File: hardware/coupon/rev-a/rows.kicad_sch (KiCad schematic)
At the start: 71 parts, among them Q1 DMP2066LSN-7, Q10 DMP2066LSN-7, Q11 DMP2066LSN-7, Q12 DMP2066LSN-7, Q13 DMP2066LSN-7, Q14 DMP2066LSN-7, Q15 DMP2066LSN-7, Q16 DMP2066LSN-7, Q17 2N7002K-7, Q18 2N7002K-7, Q19 2N7002K-7, Q2 DMP2066LSN-7, Q20 2N7002K-7, Q21 2N7002K-7, Q22 2N7002K-7, Q23 2N7002K-7, Q24 2N7002K-7, Q25 2N7002K-7, Q26 2N7002K-7, Q27 2N7002K-7, Q28 2N7002K-7, Q29 2N7002K-7, Q3 DMP2066LSN-7, Q30 2N7002K-7, Q31 2N7002K-7, Q32 2N7002K-7, Q4 DMP2066LSN-7, Q5 DMP2066LSN-7, Q6 DMP2066LSN-7, Q7 DMP2066LSN-7, Q8 DMP2066LSN-7, Q9 DMP2066LSN-7, U2 74HC4514PW,118

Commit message: Accept corrected power-library review and clear row schematic title block
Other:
- note added: "Never fabricate from this sheet alone. Real rails, VLED interlock, DRC/DFM, Gate A and timing/ghosting tests remain."
- note removed: "Never fabricate from this sheet alone. Controller, real rails, DRC/DFM, Gate A and coupon timing/ghosting tests remain."
- moved on the sheet: Q10, Q11, Q12, Q13, Q14, Q15, Q16, Q21, Q22, Q23, Q24, Q25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

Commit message: Normalize Panasonic ERJ order codes across coupon
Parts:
- R10, R11, R12, R13, R14, R15, R16, R17, R18, R19, R20, R21, R6, R7, R8, R9: symbol rgb-badge-coupon:ERJ-2RKF1001X -> rgb-badge-coupon:ERJ2RKF1001X; MPN ERJ-2RKF1001X -> ERJ2RKF1001X
- R22, R23, R24, R25, R26, R27, R28, R29, R30, R31, R32, R33, R34, R35, R36, R37, R38, R39, R40, R41, R42: symbol rgb-badge-coupon:ERJ-2RKF1003X -> rgb-badge-coupon:ERJ2RKF1003X; MPN ERJ-2RKF1003X -> ERJ2RKF1003X

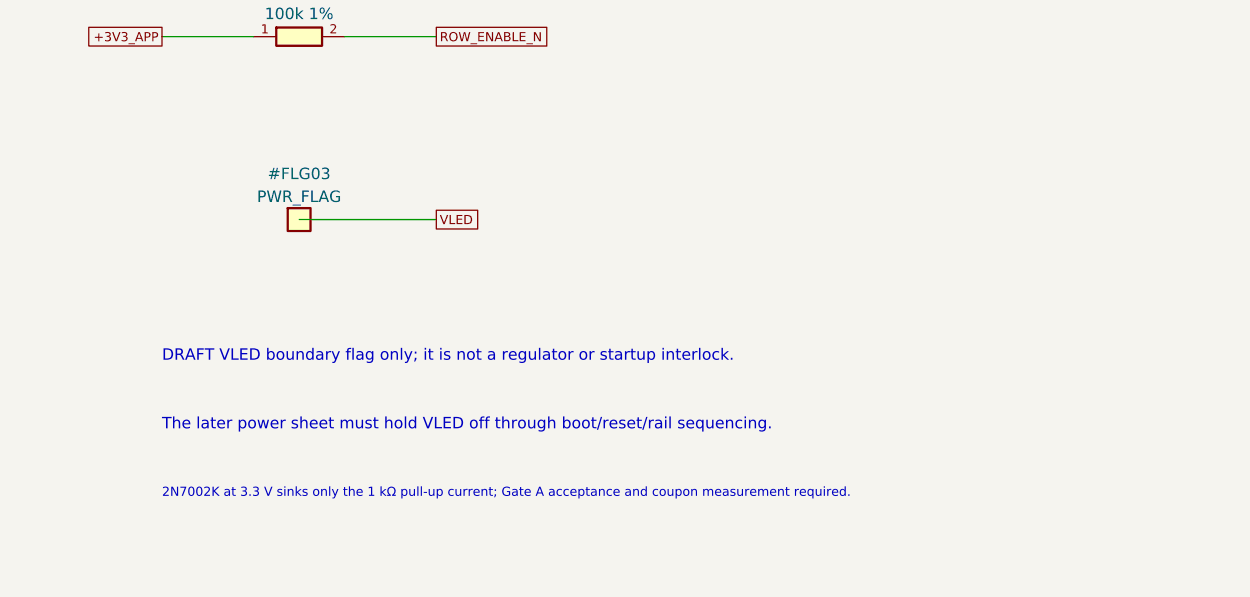
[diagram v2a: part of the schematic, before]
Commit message: Link dark VLED converter stage into coupon schematic
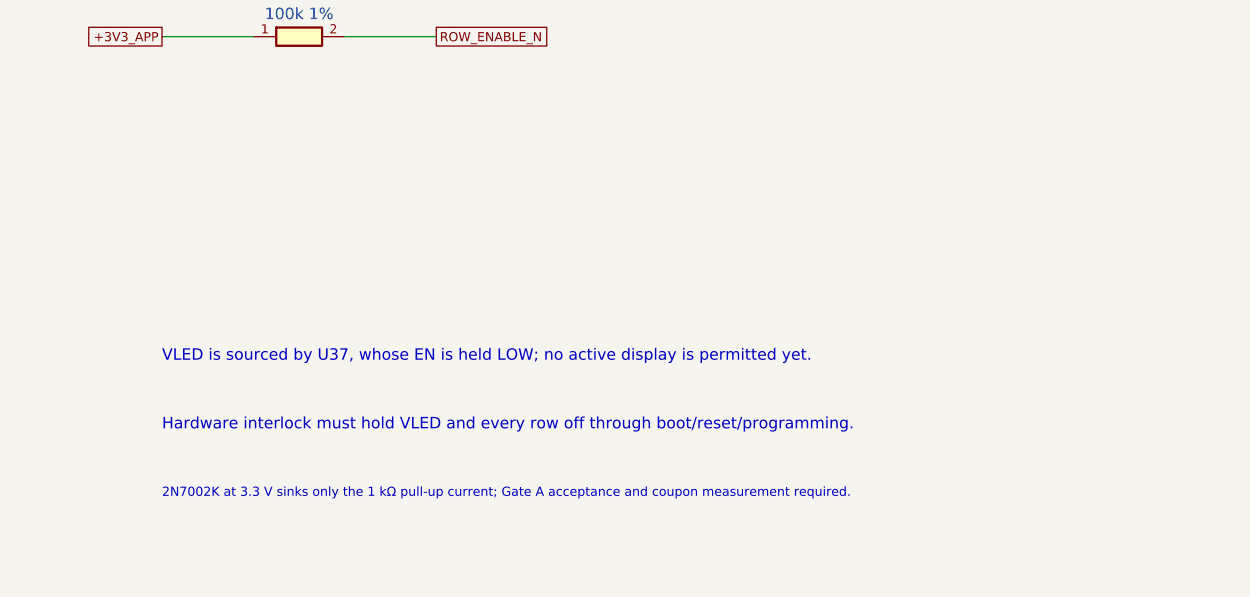
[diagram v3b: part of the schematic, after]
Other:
- note added: "Hardware interlock must hold VLED and every row off through boot/reset/programming."
- note added: "VLED is sourced by U37, whose EN is held LOW; no active display is permitted yet."
- note removed: "DRAFT VLED boundary flag only; it is not a regulator or startup interlock."
- note removed: "The later power sheet must hold VLED off through boot/reset/rail sequencing."
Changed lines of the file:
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@@
 (generator_version "1.0")
 (paper "A2")
-(title_block (title "Coupon Rev A - 16 row selectors") (rev "A-draft") (comment 1 "SPDX-License-Identifier: CERN-OHL-S-2.0") (comment 2 "Controller captured; VLED source and interlock pending"))
+(title_block (title "Coupon Rev A - 16 row selectors") (rev "A-draft") (comment 1 "SPDX-License-Identifier: CERN-OHL-S-2.0") (comment 2 "VLED stage present but held disabled; row interlock pending"))
 (text "16 decoded high-side row selectors" (at 20.32 20.32 0) (effects (font (size 2.0 2.0)) (justify left)))
 (text "E=HIGH blanks every decoder output. Firmware must blank, change A0..A3, wait, then enable." (at 20.32 27.94 0) (effects (font (size 1.27 1.27)) (justify left)))
@@
 (wire (pts (xy 198.120 38.100) (xy 208.280 38.100)) (stroke (width 0) (type default)))
 (global_label "ROW_ENABLE_N" (shape passive) (at 208.280 38.100 0) (effects (font (size 1.016 1.016)) (justify left)) (property "Intersheetrefs" "${INTERSHEET_REFS}" (at 208.280 38.100 0) (effects (font (size 1.27 1.27)) (hide yes))))
-(symbol (lib_id "rgb-badge-coupon:PWR_FLAG") (at 193.040 58.420 0) (unit 1)
-(exclude_from_sim no) (in_bom no) (on_board no) (dnp no)
-(property "Reference" "#FLG03" (at 193.040 53.340 0) (effects (font (size 1.27 1.27))))
-(property "Value" "PWR_FLAG" (at 193.040 55.880 0) (effects (font (size 1.27 1.27))))
-(property "Footprint" "" (at 193.040 58.420 0) (effects (font (size 1.27 1.27)) (hide yes)))
-(property "Datasheet" "" (at 193.040 58.420 0) (effects (font (size 1.27 1.27)) (hide yes)))
-(property "Manufacturer" "" (at 193.040 58.420 0) (effects (font (size 1.27 1.27)) (hide yes)))
-(property "MPN" "" (at 193.040 58.420 0) (effects (font (size 1.27 1.27)) (hide yes)))
-(pin "1")
-(instances (project "rgb-badge-coupon" (path "/207fb68e-2ddb-46bb-8712-eba2f8c5eef6/bb12d62e-fd97-516e-9e94-af2c7615caf5" (reference "#FLG03") (unit 1)))))
-(wire (pts (xy 193.040 58.420) (xy 208.280 58.420)) (stroke (width 0) (type default)))
-(global_label "VLED" (shape passive) (at 208.280 58.420 0) (effects (font (size 1.016 1.016)) (justify left)) (property "Intersheetrefs" "${INTERSHEET_REFS}" (at 208.280 58.420 0) (effects (font (size 1.27 1.27)) (hide yes))))
-(text "DRAFT VLED boundary flag only; it is not a regulator or startup interlock." (at 177.80 73.66 0) (effects (font (size 1.27 1.27)) (justify left)))
-(text "The later power sheet must hold VLED off through boot/reset/rail sequencing." (at 177.80 81.28 0) (effects (font (size 1.27 1.27)) (justify left)))
+(text "VLED is sourced by U37, whose EN is held LOW; no active display is permitted yet." (at 177.80 73.66 0) (effects (font (size 1.27 1.27)) (justify left)))
+(text "Hardware interlock must hold VLED and every row off through boot/reset/programming." (at 177.80 81.28 0) (effects (font (size 1.27 1.27)) (justify left)))
 (text "2N7002K at 3.3 V sinks only the 1 kΩ pull-up current; Gate A acceptance and coupon measurement required." (at 177.80 88.90 0) (effects (font (size 1.016 1.016)) (justify left)))
 (text "ROW 00" (at 33.02 111.76 0) (effects (font (size 1.27 1.27)) (justify left)))
